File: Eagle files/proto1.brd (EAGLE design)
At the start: 100 x 80 mm, 9 parts, among them U2 GY-521MPU6050, U3 HMC5883LGY-271

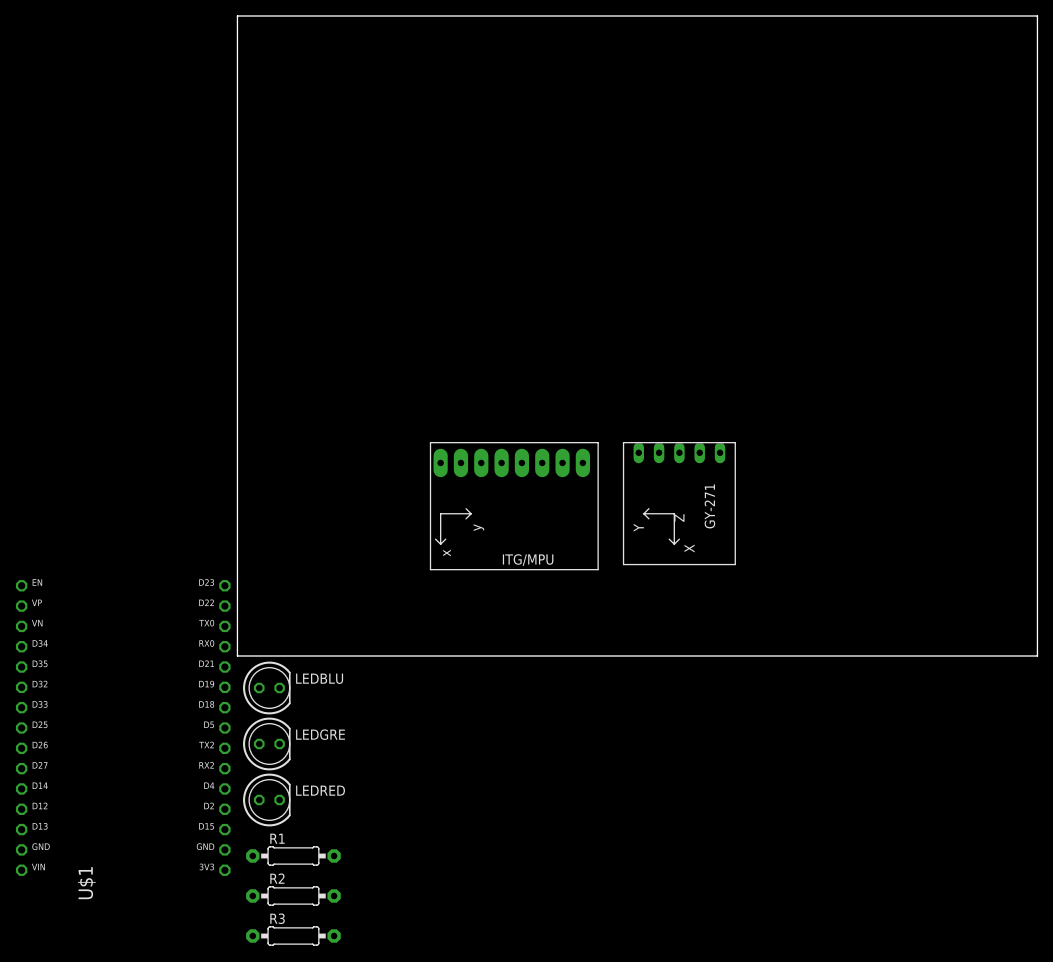
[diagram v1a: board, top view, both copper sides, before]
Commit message: Add nets
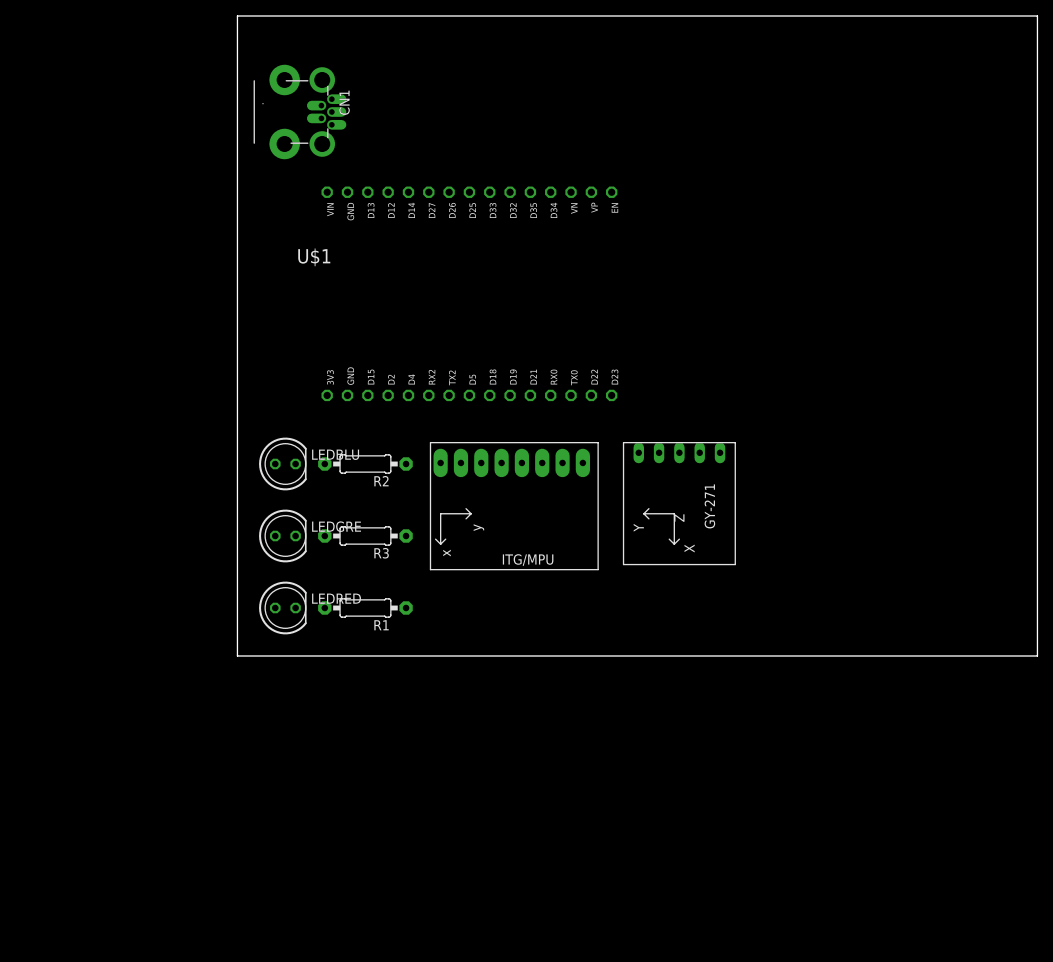
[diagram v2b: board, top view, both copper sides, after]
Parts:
- added CN1: (no value), adafruit:USB-MINIB-THM
- moved U$1 67.6 mm to (29.0, 44.0), turned to 270 degrees
- moved R2 54.7 mm to (16.0, 24.0), turned to 180 degrees
- moved R3 50.8 mm to (16.0, 15.0), turned to 180 degrees
- moved R1 32.3 mm to (16.0, 6.00), turned to 180 degrees
- moved LEDBLU 28.1 mm to (6.00, 24.0)
- moved LEDGRE 26.1 mm to (6.00, 15.0)
- moved LEDRED 24.1 mm to (6.00, 6.00)
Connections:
- removed net N$10: U3.SCL
- removed net N$11: U3.SDA
- removed net N$5: U2.XDA
- removed net N$6: U2.XCL
- new net XCL: U2.XCL, U3.SCL
- new net XDA: U2.XDA, U3.SDA
- net GND: now also CN1.GND, U$1.GND@1, U$1.GND@2
- net LEDBLU: now also U$1.D35
- net LEDGRE: now also U$1.D32
- net LEDRED: now also U$1.D34
- net SCL: now also U$1.D22
- net SDA: now also U$1.D21
- net VCC: now also CN1.VBUS, U$1.3V3
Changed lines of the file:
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@@
 <element name="U2" library="gy-521" package="GY-521" value="GY-521MPU6050" x="34.29" y="15.24" smashed="yes" rot="R270"/>
 <element name="U3" library="hmc5883l" package="GY-271" value="HMC5883LGY-271" x="54.61" y="19.05" smashed="yes" rot="R270"/>
-<element name="LEDBLU" library="led" library_urn="urn:adsk.eagle:library:259" package="LED5MM" package3d_urn="urn:adsk.eagle:package:15799/2" value="" x="4" y="-4" smashed="yes">
-<attribute name="NAME" x="7.175" y="-3.4666" size="1.27" layer="25" ratio="10"/>
-<attribute name="POPULARITY" value="93" x="4" y="-4" size="1.778" layer="27" display="off"/>
-<attribute name="VALUE" x="7.2004" y="-5.8034" size="1.27" layer="27" ratio="10"/>
+<element name="LEDBLU" library="led" library_urn="urn:adsk.eagle:library:259" package="LED5MM" package3d_urn="urn:adsk.eagle:package:15799/2" value="" x="6" y="24" smashed="yes">
+<attribute name="NAME" x="9.175" y="24.5334" size="1.27" layer="25" ratio="10"/>
+<attribute name="POPULARITY" value="93" x="6" y="24" size="1.778" layer="27" display="off"/>
+<attribute name="VALUE" x="9.2004" y="22.1966" size="1.27" layer="27" ratio="10"/>
 </element>
-<element name="LEDGRE" library="led" library_urn="urn:adsk.eagle:library:259" package="LED5MM" package3d_urn="urn:adsk.eagle:package:15799/2" value="" x="4" y="-11" smashed="yes">
-<attribute name="NAME" x="7.175" y="-10.4666" size="1.27" layer="25" ratio="10"/>
-<attribute name="POPULARITY" value="93" x="4" y="-11" size="1.778" layer="27" display="off"/>
-<attribute name="VALUE" x="7.2004" y="-12.8034" size="1.27" layer="27" ratio="10"/>
+<element name="LEDGRE" library="led" library_urn="urn:adsk.eagle:library:259" package="LED5MM" package3d_urn="urn:adsk.eagle:package:15799/2" value="" x="6" y="15" smashed="yes">
+<attribute name="NAME" x="9.175" y="15.5334" size="1.27" layer="25" ratio="10"/>
+<attribute name="POPULARITY" value="93" x="6" y="15" size="1.778" layer="27" display="off"/>
+<attribute name="VALUE" x="9.2004" y="13.1966" size="1.27" layer="27" ratio="10"/>
 </element>
-<element name="LEDRED" library="led" library_urn="urn:adsk.eagle:library:259" package="LED5MM" package3d_urn="urn:adsk.eagle:package:15799/2" value="" x="4" y="-18" smashed="yes">
-<attribute name="NAME" x="7.175" y="-17.4666" size="1.27" layer="25" ratio="10"/>
-<attribute name="POPULARITY" value="93" x="4" y="-18" size="1.778" layer="27" display="off"/>
-<attribute name="VALUE" x="7.2004" y="-19.8034" size="1.27" layer="27" ratio="10"/>
+<element name="LEDRED" library="led" library_urn="urn:adsk.eagle:library:259" package="LED5MM" package3d_urn="urn:adsk.eagle:package:15799/2" value="" x="6" y="6" smashed="yes">
+<attribute name="NAME" x="9.175" y="6.5334" size="1.27" layer="25" ratio="10"/>
+<attribute name="POPULARITY" value="93" x="6" y="6" size="1.778" layer="27" display="off"/>
+<attribute name="VALUE" x="9.2004" y="4.1966" size="1.27" layer="27" ratio="10"/>
 </element>
-<element name="R1" library="adafruit" package="0207/10" value="" x="7" y="-25" smashed="yes">
-<attribute name="NAME" x="3.952" y="-23.476" size="1.27" layer="25" ratio="10"/>
-<attribute name="VALUE" x="4.7394" y="-25.635" size="1.27" layer="27" ratio="10"/>
+<element name="R1" library="adafruit" package="0207/10" value="" x="16" y="6" smashed="yes" rot="R180">
+<attribute name="NAME" x="19.048" y="4.476" size="1.27" layer="25" ratio="10" rot="R180"/>
+<attribute name="VALUE" x="18.2606" y="6.635" size="1.27" layer="27" ratio="10" rot="R180"/>
 </element>
-<element name="R2" library="adafruit" package="0207/10" value="" x="7" y="-30" smashed="yes">
-<attribute name="NAME" x="3.952" y="-28.476" size="1.27" layer="25" ratio="10"/>
-<attribute name="VALUE" x="4.7394" y="-30.635" size="1.27" layer="27" ratio="10"/>
+<element name="R2" library="adafruit" package="0207/10" value="" x="16" y="24" smashed="yes" rot="R180">
+<attribute name="NAME" x="19.048" y="22.476" size="1.27" layer="25" ratio="10" rot="R180"/>
+<attribute name="VALUE" x="18.2606" y="24.635" size="1.27" layer="27" ratio="10" rot="R180"/>
 </element>
-<element name="R3" library="adafruit" package="0207/10" value="" x="7" y="-35" smashed="yes">
-<attribute name="NAME" x="3.952" y="-33.476" size="1.27" layer="25" ratio="10"/>
-<attribute name="VALUE" x="4.7394" y="-35.635" size="1.27" layer="27" ratio="10"/>
+<element name="R3" library="adafruit" package="0207/10" value="" x="16" y="15" smashed="yes" rot="R180">
+<attribute name="NAME" x="19.048" y="13.476" size="1.27" layer="25" ratio="10" rot="R180"/>
+<attribute name="VALUE" x="18.2606" y="15.635" size="1.27" layer="27" ratio="10" rot="R180"/>
 </element>
-<element name="U$1" library="DOIT_ESP32_DEVKIT" package="ESP32_DEVKIT" value="ESP32_DEVKIT" x="-13" y="-9" smashed="yes">
-<attribute name="NAME" x="-18.08" y="-30.59" size="1.778" layer="25" rot="R90"/>
-<attribute name="VALUE" x="-9.19" y="-30.59" size="1.778" layer="27" rot="R90"/>
+<element name="U$1" library="DOIT_ESP32_DEVKIT" package="ESP32_DEVKIT" value="ESP32_DEVKIT" x="29" y="44" smashed="yes" rot="R270">
+<attribute name="NAME" x="7.41" y="49.08" size="1.778" layer="25"/>
+<attribute name="VALUE" x="7.41" y="40.19" size="1.778" layer="27"/>
+</element>
+<element name="CN1" library="adafruit" package="USB-MINIB-THM" value="" x="2" y="68" smashed="yes" rot="R270">
+<attribute name="NAME" x="12.75" y="70.81" size="1.27" layer="25" font="vector" rot="R270"/>
+<attribute name="VALUE" x="0.35" y="71.31" size="1.27" layer="27" font="vector" rot="R270"/>
 </element>
 </elements>
@@
 <contactref element="U2" pad="GND"/>
 <contactref element="U3" pad="GND"/>
+<contactref element="U$1" pad="GND@1"/>
+<contactref element="U$1" pad="GND@2"/>
+<contactref element="CN1" pad="GND"/>
 <wire x1="40.64" y1="24.13" x2="57.785" y2="25.4" width="0" layer="19" extent="1-1"/>
+<wire x1="13.76" y1="32.57" x2="40.64" y2="24.13" width="0" layer="19" extent="1-1"/>
+<wire x1="13.76" y1="57.97" x2="13.76" y2="32.57" width="0" layer="19" extent="1-1"/>
+<wire x1="11.8" y1="66.4" x2="13.76" y2="32.57" width="0" layer="19" extent="1-1"/>
 </signal>
 <signal name="SCL">
 <contactref element="U2" pad="SCL"/>
+<contactref element="U$1" pad="D22"/>
+<wire x1="44.24" y1="32.57" x2="38.1" y2="24.13" width="0" layer="19" extent="1-1"/>
 </signal>
 <signal name="SDA">
 <contactref element="U2" pad="SDA"/>
+<contactref element="U$1" pad="D21"/>
+<wire x1="36.62" y1="32.57" x2="35.56" y2="24.13" width="0" layer="19" extent="1-1"/>
 </signal>
-<signal name="N$5">
+<signal name="XDA">
 <contactref element="U2" pad="XDA"/>
+<contactref element="U3" pad="SDA"/>
+<wire x1="33.02" y1="24.13" x2="52.705" y2="25.4" width="0" layer="19" extent="1-1"/>
 </signal>
-<signal name="N$6">
+<signal name="XCL">
 <contactref element="U2" pad="XCL"/>
+<contactref element="U3" pad="SCL"/>
+<wire x1="30.48" y1="24.13" x2="55.245" y2="25.4" width="0" layer="19" extent="1-1"/>
 </signal>
 <signal name="VCC">
@@
 <contactref element="LEDBLU" pad="A"/>
 <contactref element="LEDGRE" pad="A"/>
+<contactref element="U$1" pad="3V3"/>
+<contactref element="CN1" pad="VBUS"/>
 <wire x1="43.18" y1="24.13" x2="60.325" y2="25.4" width="0" layer="19" extent="1-1"/>
-<wire x1="2.73" y1="-4" x2="43.18" y2="24.13" width="0" layer="19" extent="1-1"/>
-<wire x1="2.73" y1="-11" x2="2.73" y2="-4" width="0" layer="19" extent="1-1"/>
-<wire x1="2.73" y1="-18" x2="2.73" y2="-11" width="0" layer="19" extent="1-1"/>
-</signal>
-<signal name="N$10">
-<contactref element="U3" pad="SCL"/>
-</signal>
-<signal name="N$11">
-<contactref element="U3" pad="SDA"/>
+<wire x1="11.22" y1="32.57" x2="43.18" y2="24.13" width="0" layer="19" extent="1-1"/>
+<wire x1="4.73" y1="24" x2="11.22" y2="32.57" width="0" layer="19" extent="1-1"/>
+<wire x1="4.73" y1="15" x2="4.73" y2="24" width="0" layer="19" extent="1-1"/>
+<wire x1="4.73" y1="6" x2="4.73" y2="15" width="0" layer="19" extent="1-1"/>
+<wire x1="11.8" y1="69.6" x2="4.73" y2="15" width="0" layer="19" extent="1-1"/>
 </signal>
 <signal name="LEDGRE">
 <contactref element="R3" pad="1"/>
+<contactref element="U$1" pad="D32"/>
+<wire x1="34.08" y1="57.97" x2="21.08" y2="15" width="0" layer="19" extent="1-1"/>
 </signal>
 <signal name="LEDRED">
 <contactref element="R1" pad="1"/>
+<contactref element="U$1" pad="D34"/>
+<wire x1="21.08" y1="6" x2="39.16" y2="57.97" width="0" layer="19" extent="1-1"/>
 </signal>
 <signal name="LEDBLU">
 <contactref element="R2" pad="1"/>
+<contactref element="U$1" pad="D35"/>
+<wire x1="36.62" y1="57.97" x2="21.08" y2="24" width="0" layer="19" extent="1-1"/>
 </signal>
 <signal name="N$1">
 <contactref element="LEDRED" pad="K"/>
 <contactref element="R1" pad="2"/>
-<wire x1="12.08" y1="-25" x2="5.27" y2="-18" width="0" layer="19" extent="1-1"/>
+<wire x1="10.92" y1="6" x2="7.27" y2="6" width="0" layer="19" extent="1-1"/>
 </signal>
 <signal name="N$3">
 <contactref element="LEDBLU" pad="K"/>
 <contactref element="R2" pad="2"/>
-<wire x1="5.27" y1="-4" x2="12.08" y2="-30" width="0" layer="19" extent="1-1"/>
+<wire x1="7.27" y1="24" x2="10.92" y2="24" width="0" layer="19" extent="1-1"/>
 </signal>
 <signal name="N$4">
 <contactref element="LEDGRE" pad="K"/>
 <contactref element="R3" pad="2"/>
-<wire x1="5.27" y1="-11" x2="12.08" y2="-35" width="0" layer="19" extent="1-1"/>
+<wire x1="7.27" y1="15" x2="10.92" y2="15" width="0" layer="19" extent="1-1"/>
 </signal>
 </signals>

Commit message: Add MPU-9250
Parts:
- removed U2: GY-521MPU6050, gy-521:GY-521
- removed U3: HMC5883LGY-271, hmc5883l:GY-271
- added U$2: GY-9250, GY-9250:GY-9250
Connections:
- removed net XCL: U2.XCL, U3.SCL
- removed net XDA: U2.XDA, U3.SDA
- net GND: now also U$2.GND; no longer U2.GND, U3.GND
- net SCL: now also U$2.SCL; no longer U2.SCL
- net SDA: now also U$2.SDA; no longer U2.SDA
- net VCC: now also U$2.VCC; no longer U2.VCC, U3.VCC
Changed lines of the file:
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@@
 </autorouter>
 <elements>
-<element name="U2" library="gy-521" package="GY-521" value="GY-521MPU6050" x="34.29" y="15.24" smashed="yes" rot="R270"/>
-<element name="U3" library="hmc5883l" package="GY-271" value="HMC5883LGY-271" x="54.61" y="19.05" smashed="yes" rot="R270"/>
 <element name="LEDBLU" library="led" library_urn="urn:adsk.eagle:library:259" package="LED5MM" package3d_urn="urn:adsk.eagle:package:15799/2" value="" x="6" y="24" smashed="yes">
 <attribute name="NAME" x="9.175" y="24.5334" size="1.27" layer="25" ratio="10"/>
@@
 <attribute name="VALUE" x="0.35" y="71.31" size="1.27" layer="27" font="vector" rot="R270"/>
 </element>
+<element name="U$2" library="GY-9250" package="GY-9250" value="GY-9250" x="-16" y="1" smashed="yes"/>
 </elements>
 <signals>
 <signal name="GND">
-<contactref element="U2" pad="GND"/>
-<contactref element="U3" pad="GND"/>
 <contactref element="U$1" pad="GND@1"/>
 <contactref element="U$1" pad="GND@2"/>
 <contactref element="CN1" pad="GND"/>
-<wire x1="40.64" y1="24.13" x2="57.785" y2="25.4" width="0" layer="19" extent="1-1"/>
-<wire x1="13.76" y1="32.57" x2="40.64" y2="24.13" width="0" layer="19" extent="1-1"/>
-<wire x1="13.76" y1="57.97" x2="13.76" y2="32.57" width="0" layer="19" extent="1-1"/>
-<wire x1="11.8" y1="66.4" x2="13.76" y2="32.57" width="0" layer="19" extent="1-1"/>
+<contactref element="U$2" pad="GND"/>
+<wire x1="13.76" y1="57.97" x2="11.8" y2="66.4" width="0" layer="19" extent="1-1"/>
+<wire x1="13.76" y1="32.57" x2="13.76" y2="57.97" width="0" layer="19" extent="1-1"/>
+<wire x1="-15" y1="22.46" x2="13.76" y2="32.57" width="0" layer="19" extent="1-1"/>
 </signal>
 <signal name="SCL">
-<contactref element="U2" pad="SCL"/>
 <contactref element="U$1" pad="D22"/>
-<wire x1="44.24" y1="32.57" x2="38.1" y2="24.13" width="0" layer="19" extent="1-1"/>
+<contactref element="U$2" pad="SCL"/>
+<wire x1="-15" y1="19.92" x2="44.24" y2="32.57" width="0" layer="19" extent="1-1"/>
 </signal>
 <signal name="SDA">
-<contactref element="U2" pad="SDA"/>
 <contactref element="U$1" pad="D21"/>
-<wire x1="36.62" y1="32.57" x2="35.56" y2="24.13" width="0" layer="19" extent="1-1"/>
-</signal>
-<signal name="XDA">
-<contactref element="U2" pad="XDA"/>
-<contactref element="U3" pad="SDA"/>
-<wire x1="33.02" y1="24.13" x2="52.705" y2="25.4" width="0" layer="19" extent="1-1"/>
-</signal>
-<signal name="XCL">
-<contactref element="U2" pad="XCL"/>
-<contactref element="U3" pad="SCL"/>
-<wire x1="30.48" y1="24.13" x2="55.245" y2="25.4" width="0" layer="19" extent="1-1"/>
+<contactref element="U$2" pad="SDA"/>
+<wire x1="-15" y1="17.38" x2="36.62" y2="32.57" width="0" layer="19" extent="1-1"/>
 </signal>
 <signal name="VCC">
-<contactref element="U2" pad="VCC"/>
-<contactref element="U3" pad="VCC"/>
 <contactref element="LEDRED" pad="A"/>
 <contactref element="LEDBLU" pad="A"/>
@@
 <contactref element="U$1" pad="3V3"/>
 <contactref element="CN1" pad="VBUS"/>
-<wire x1="43.18" y1="24.13" x2="60.325" y2="25.4" width="0" layer="19" extent="1-1"/>
-<wire x1="11.22" y1="32.57" x2="43.18" y2="24.13" width="0" layer="19" extent="1-1"/>
+<contactref element="U$2" pad="VCC"/>
+<wire x1="11.22" y1="32.57" x2="11.8" y2="69.6" width="0" layer="19" extent="1-1"/>
 <wire x1="4.73" y1="24" x2="11.22" y2="32.57" width="0" layer="19" extent="1-1"/>
 <wire x1="4.73" y1="15" x2="4.73" y2="24" width="0" layer="19" extent="1-1"/>
 <wire x1="4.73" y1="6" x2="4.73" y2="15" width="0" layer="19" extent="1-1"/>
-<wire x1="11.8" y1="69.6" x2="4.73" y2="15" width="0" layer="19" extent="1-1"/>
+<wire x1="-15" y1="25" x2="4.73" y2="24" width="0" layer="19" extent="1-1"/>
 </signal>
 <signal name="LEDGRE">
